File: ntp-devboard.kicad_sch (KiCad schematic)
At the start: 71 parts, among them J1 USB_C_Receptacle_USB2.0_14P, J2 Conn_01x07, J3 Conn_01x20, J4 Conn_01x04, J6 RJ45_Hanrun_HR911105A_Horizon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, SW1 SW_Push, U1 RP2040, U2 MCP1700x-330xxTT, U3 LAN9250/ML, U4 W25Q16JVUXIQ TR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

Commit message: bom optimisation
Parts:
- C37: footprint Capacitor_SMD:C_0402_1005Metric -> Capacitor_SMD:C_0805_2012Metric
- FB1, FB2, FB3, FB4: footprint Inductor_SMD:L_0201_0603Metric -> Inductor_SMD:L_0603_1608Metric
- R11, R12: value 330 -> 10K
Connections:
- no-connect marks 24 -> 23
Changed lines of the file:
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@@
 	)
 	(no_connect
-		(at 25.4 135.89)
-	)
-	(no_connect
 		(at 35.56 254)
 	)
@@
 			)
 		)
-		(property "Value" "330"
+		(property "Value" "10K"
 			(at 151.13 264.16 90)
 			(effects
@@
 			)
 		)
-		(property "Footprint" "Inductor_SMD:L_0201_0603Metric"
+		(property "Footprint" "Inductor_SMD:L_0603_1608Metric"
 			(at 313.182 163.83 90)
 			(effects
@@
 			)
 		)
-		(property "Value" "330"
+		(property "Value" "10K"
 			(at 19.05 228.6 90)
 			(effects
@@
 			)
 		)
-		(property "Footprint" "Inductor_SMD:L_0201_0603Metric"
+		(property "Footprint" "Inductor_SMD:L_0603_1608Metric"
 			(at 245.872 236.22 90)
 			(effects
@@
 			)
 		)
-		(property "Footprint" "Inductor_SMD:L_0201_0603Metric"
+		(property "Footprint" "Inductor_SMD:L_0603_1608Metric"
 			(at 341.122 163.83 90)
 			(effects
@@
 			)
 		)
-		(property "Footprint" "Capacitor_SMD:C_0402_1005Metric"
+		(property "Footprint" "Capacitor_SMD:C_0805_2012Metric"
 			(at 284.1752 240.03 0)
 			(effects
@@
 			)
 		)
-		(property "Footprint" "Inductor_SMD:L_0201_0603Metric"
+		(property "Footprint" "Inductor_SMD:L_0603_1608Metric"
 			(at 328.422 163.83 90)
 			(effects

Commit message: uhm, _minor_ mistake
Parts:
- added J5: Conn_01x02, Connector_PinHeader_2.54mm:PinHeader_1x02_P2.54mm_Vertical, symbol Connector_Generic:Conn_01x02
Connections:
- net GND: no longer J6.10, J6.11
- net LAN45: now also J5.2 (Pin_2); no longer J6.9
- net LAN46: now also J5.1 (Pin_1); no longer J6.12
- no-connect marks 23 -> 28
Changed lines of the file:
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@@
 	)
 	(no_connect
+		(at 224.79 220.98)
+	)
+	(no_connect
 		(at 35.56 251.46)
 	)
@@
 	)
 	(no_connect
+		(at 224.79 218.44)
+	)
+	(no_connect
+		(at 224.79 223.52)
+	)
+	(no_connect
 		(at 35.56 241.3)
 	)
@@
 	)
 	(no_connect
+		(at 224.79 208.28)
+	)
+	(no_connect
 		(at 35.56 215.9)
 	)
@@
 	)
 	(no_connect
+		(at 224.79 210.82)
+	)
+	(no_connect
 		(at 35.56 238.76)
 	)
@@
 		)
 	)
-	(global_label "LAN46"
-		(shape input)
-		(at 224.79 208.28 0)
-		(fields_autoplaced yes)
-		(effects
-			(font
-				(size 1.27 1.27)
-			)
-			(justify left)
-		)
-		(property "Intersheetrefs" "${INTERSHEET_REFS}"
-			(at 233.6414 208.28 0)
-			(effects
-				(font
-					(size 1.27 1.27)
-				)
-				(justify left)
-				(hide yes)
-			)
-		)
-	)
 	(global_label "QSPI_SD0"
 		(shape bidirectional)
@@
 		)
 	)
+	(global_label "LAN45"
+		(shape input)
+		(at 39.37 121.92 180)
+		(fields_autoplaced yes)
+		(effects
+			(font
+				(size 1.27 1.27)
+			)
+			(justify right)
+		)
+		(property "Intersheetrefs" "${INTERSHEET_REFS}"
+			(at 30.5186 121.92 0)
+			(effects
+				(font
+					(size 1.27 1.27)
+				)
+				(justify right)
+				(hide yes)
+			)
+		)
+	)
 	(global_label "GPIO28_ADC2"
 		(shape bidirectional)
@@
 		)
 	)
-	(global_label "LAN45"
-		(shape input)
-		(at 224.79 218.44 0)
-		(fields_autoplaced yes)
-		(effects
-			(font
-				(size 1.27 1.27)
-			)
-			(justify left)
-		)
-		(property "Intersheetrefs" "${INTERSHEET_REFS}"
-			(at 233.6414 218.44 0)
-			(effects
-				(font
-					(size 1.27 1.27)
-				)
-				(justify left)
-				(hide yes)
-			)
-		)
-	)
 	(global_label "GPIO17"
 		(shape bidirectional)
@@
 		)
 	)
+	(global_label "LAN46"
+		(shape input)
+		(at 39.37 119.38 180)
+		(fields_autoplaced yes)
+		(effects
+			(font
+				(size 1.27 1.27)
+			)
+			(justify right)
+		)
+		(property "Intersheetrefs" "${INTERSHEET_REFS}"
+			(at 30.5186 119.38 0)
+			(effects
+				(font
+					(size 1.27 1.27)
+				)
+				(justify right)
+				(hide yes)
+			)
+		)
+	)
 	(global_label "QSPI_SD3"
 		(shape bidirectional)
@@
 	)
 	(symbol
-		(lib_id "power:+3V3")
-		(at 327.66 153.67 0)
+		(lib_id "Connector_Generic:Conn_01x02")
+		(at 44.45 119.38 0)
 		(unit 1)
 		(exclude_from_sim no)
@@
 		(dnp no)
 		(fields_autoplaced yes)
-		(property "Reference" "#PWR046"
-			(at 327.66 157.48 0)
+		(property "Reference" "J5"
+			(at 46.99 119.3799 0)
 			(effects
 				(font
 					(size 1.27 1.27)
 				)
-				(hide yes)
+				(justify left)
 			)
 		)
-		(property "Value" "+3V3"
-			(at 327.66 148.59 0)
+		(property "Value" "Conn_01x02"
+			(at 46.99 121.9199 0)
 			(effects
 				(font
 					(size 1.27 1.27)
 				)
+				(justify left)
 			)
 		)
-		(property "Footprint" ""
-			(at 327.66 153.67 0)
+		(property "Footprint" "Connector_PinHeader_2.54mm:PinHeader_1x02_P2.54mm_Vertical"
+			(at 44.45 119.38 0)
 			(effects
 				(font
@@
 			)
 		)
-		(property "Datasheet" ""
-			(at 327.66 153.67 0)
+		(property "Datasheet" "~"
+			(at 44.45 119.38 0)
 			(effects
 				(font
@@
 			)
 		)
-		(property "Description" "Power symbol creates a global label with name \"+3V3\""
-			(at 327.66 153.67 0)
+		(property "Description" "Generic connector, single row, 01x02, script generated (kicad-library-utils/schlib/autogen/connector/)"
+			(at 44.45 119.38 0)
 			(effects
 				(font
@@
 		(pin "1"
 		)
+		(pin "2"
+		)
 		(instances
-			(project "ntp-devboard"
+			(project ""
 				(path "/8a2a4d17-ab41-4dea-99ab-88cd6502c408"
-					(reference "#PWR046")
+					(reference "J5")
 					(unit 1)
 				)
@@
 	)
 	(symbol
-		(lib_id "Device:R")
-		(at 168.91 194.31 270)
+		(lib_id "power:+3V3")
+		(at 327.66 153.67 0)
 		(unit 1)
 		(exclude_from_sim no)
@@
 		(on_board yes)
 		(dnp no)
-		(property "Reference" "R15"
-			(at 168.91 189.23 90)
+		(fields_autoplaced yes)
+		(property "Reference" "#PWR046"
+			(at 327.66 157.48 0)
 			(effects
 				(font
 					(size 1.27 1.27)
 				)
+				(hide yes)
 			)
 		)
-		(property "Value" "12.1K"
-			(at 168.91 191.77 90)
+		(property "Value" "+3V3"
+			(at 327.66 148.59 0)
 			(effects
 				(font
@@
 			)
 		)
-		(property "Footprint" "Resistor_SMD:R_0402_1005Metric"
-			(at 168.91 192.532 90)
+		(property "Footprint" ""
+			(at 327.66 153.67 0)
 			(effects
 				(font
@@
 			)
 		)
-		(property "Datasheet" "~"
-			(at 168.91 194.31 0)
+		(property "Datasheet" ""
+			(at 327.66 153.67 0)
 			(effects
 				(font
@@
 			)
 		)
-		(property "Description" "Resistor"
-			(at 168.91 194.31 0)
+		(property "Description" "Power symbol creates a global label with name \"+3V3\""
+			(at 327.66 153.67 0)
 			(effects
 				(font
@@
 			)
 		)
-		(pin "2"
-		)
 		(pin "1"
 		)
@@
 			(project "ntp-devboard"
 				(path "/8a2a4d17-ab41-4dea-99ab-88cd6502c408"
-					(reference "R15")
+					(reference "#PWR046")
 					(unit 1)
 				)
@@
 	)
 	(symbol
-		(lib_id "power:GND")
-		(at 224.79 210.82 0)
+		(lib_id "Device:R")
+		(at 168.91 194.31 270)
 		(unit 1)
 		(exclude_from_sim no)
@@
 		(on_board yes)
 		(dnp no)
-		(fields_autoplaced yes)
-		(property "Reference" "#PWR036"
-			(at 224.79 217.17 0)
+		(property "Reference" "R15"
+			(at 168.91 189.23 90)
 			(effects
 				(font
 					(size 1.27 1.27)
 				)
-				(hide yes)
 			)
 		)
-		(property "Value" "GND"
-			(at 224.79 215.9 0)
+		(property "Value" "12.1K"
+			(at 168.91 191.77 90)
 			(effects
 				(font
@@
 			)
 		)
-		(property "Footprint" ""
-			(at 224.79 210.82 0)
+		(property "Footprint" "Resistor_SMD:R_0402_1005Metric"
+			(at 168.91 192.532 90)
 			(effects
 				(font
@@
 			)
 		)
-		(property "Datasheet" ""
-			(at 224.79 210.82 0)
+		(property "Datasheet" "~"
+			(at 168.91 194.31 0)
 			(effects
 				(font
@@
 			)
 		)
-		(property "Description" "Power symbol creates a global label with name \"GND\" , ground"
-			(at 224.79 210.82 0)
+		(property "Description" "Resistor"
+			(at 168.91 194.31 0)
 			(effects
 				(font
@@
 			)
 		)
+		(pin "2"
+		)
 		(pin "1"
 		)
@@
 			(project "ntp-devboard"
 				(path "/8a2a4d17-ab41-4dea-99ab-88cd6502c408"
-					(reference "#PWR036")
+					(reference "R15")
 					(unit 1)
 				)
@@
 					(unit 1)
 				)
-			)
-		)
-	)
-	(symbol
-		(lib_id "power:GND")
-		(at 224.79 220.98 0)
-		(unit 1)
-		(exclude_from_sim no)
-		(in_bom yes)
-		(on_board yes)
-		(dnp no)
-		(fields_autoplaced yes)
-		(property "Reference" "#PWR035"
-			(at 224.79 227.33 0)
-			(effects
-				(font
-					(size 1.27 1.27)
-				)
-				(hide yes)
-			)
-		)
-		(property "Value" "GND"
-			(at 224.79 226.06 0)
-			(effects
-				(font
-					(size 1.27 1.27)
-				)
-			)
-		)
-		(property "Footprint" ""
-			(at 224.79 220.98 0)
-			(effects
-				(font
-					(size 1.27 1.27)
-				)
-				(hide yes)
-			)
-		)
-		(property "Datasheet" ""
-			(at 224.79 220.98 0)
-			(effects
-				(font
-					(size 1.27 1.27)
-				)
-				(hide yes)
-			)
-		)
-		(property "Description" "Power symbol creates a global label with name \"GND\" , ground"
-			(at 224.79 220.98 0)
-			(effects
-				(font
-					(size 1.27 1.27)
-				)
-				(hide yes)
-			)
-		)
-		(pin "1"
-		)
-		(instances
-			(project "ntp-devboard"
-				(path "/8a2a4d17-ab41-4dea-99ab-88cd6502c408"
-					(reference "#PWR035")
-					(unit 1)
-				)

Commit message: cooked ah decoupling caps
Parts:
- C18, C19: value 33pF -> 15pF
- R15: value 12.1K -> 12K
- R3, R4: value 27 -> 22
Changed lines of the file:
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@@
 			)
 		)
-		(property "Value" "27"
+		(property "Value" "22"
 			(at 133.35 68.834 90)
 			(effects
@@
 			)
 		)
-		(property "Value" "27"
+		(property "Value" "22"
 			(at 133.35 77.216 90)
 			(effects
@@
 			)
 		)
-		(property "Value" "12.1K"
+		(property "Value" "12K"
 			(at 168.91 191.77 90)
 			(effects
@@
 			)
 		)
-		(property "Value" "33pF"
+		(property "Value" "15pF"
 			(at 233.68 138.684 90)
 			(effects
@@
 			)
 		)
-		(property "Value" "33pF"
+		(property "Value" "15pF"
 			(at 233.68 148.844 90)
 			(effects

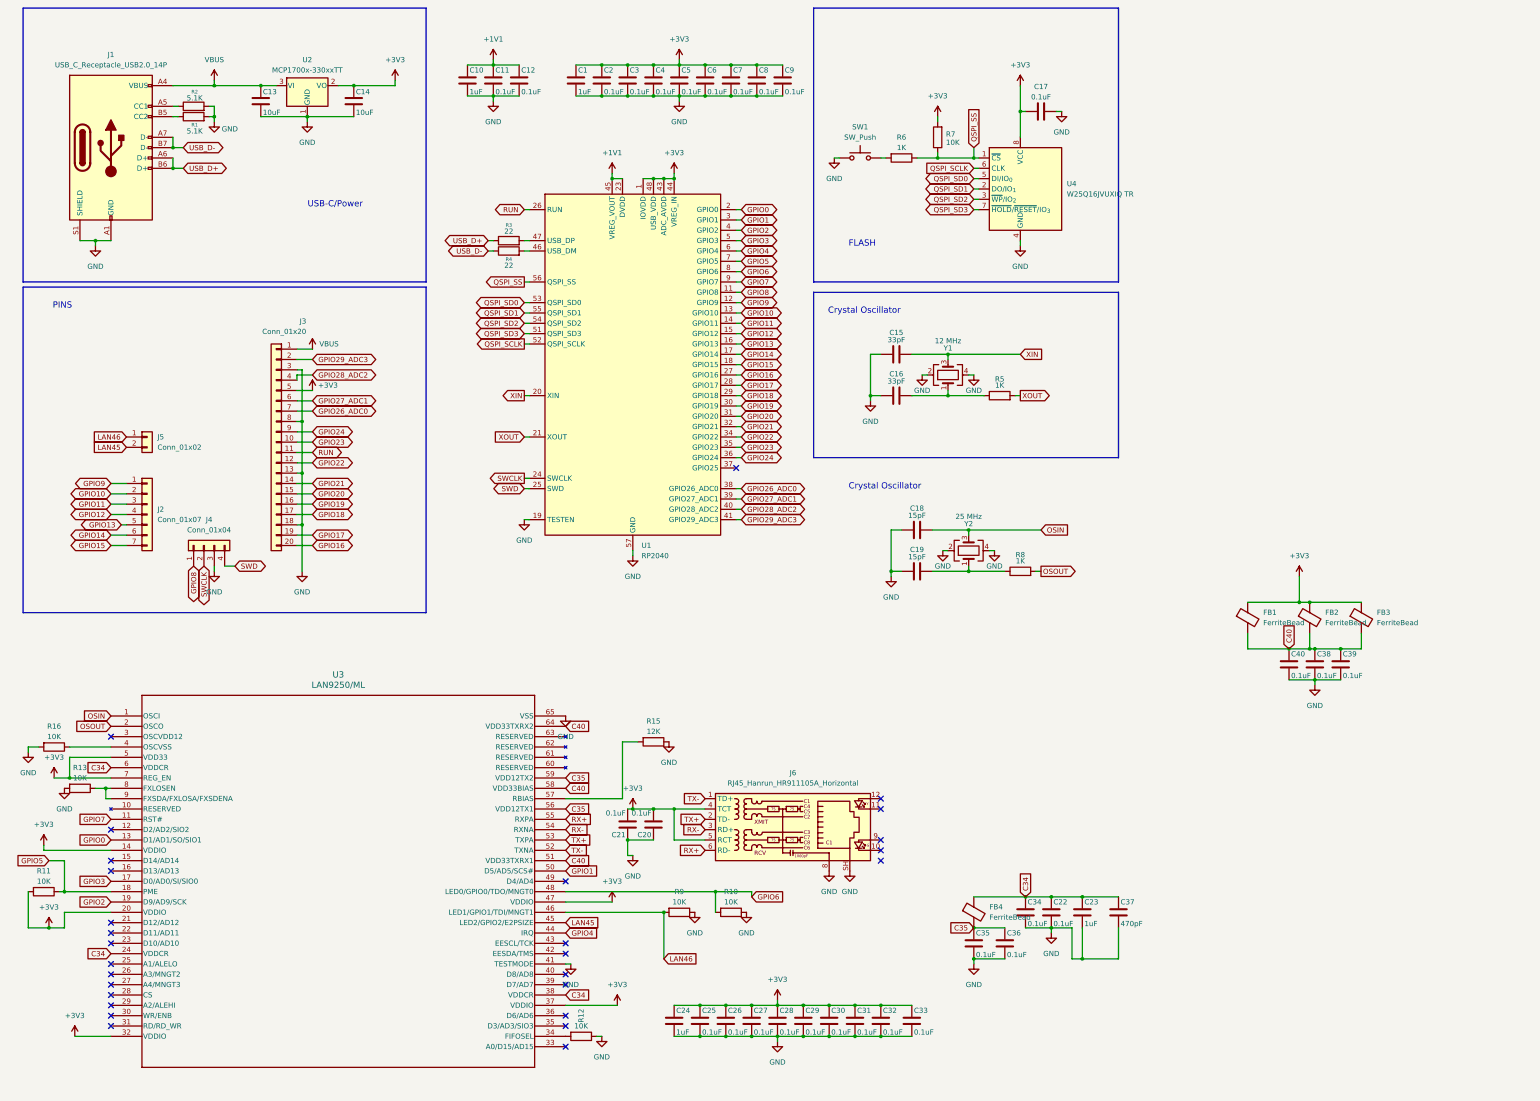
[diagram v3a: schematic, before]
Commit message: Improved schematic readbility
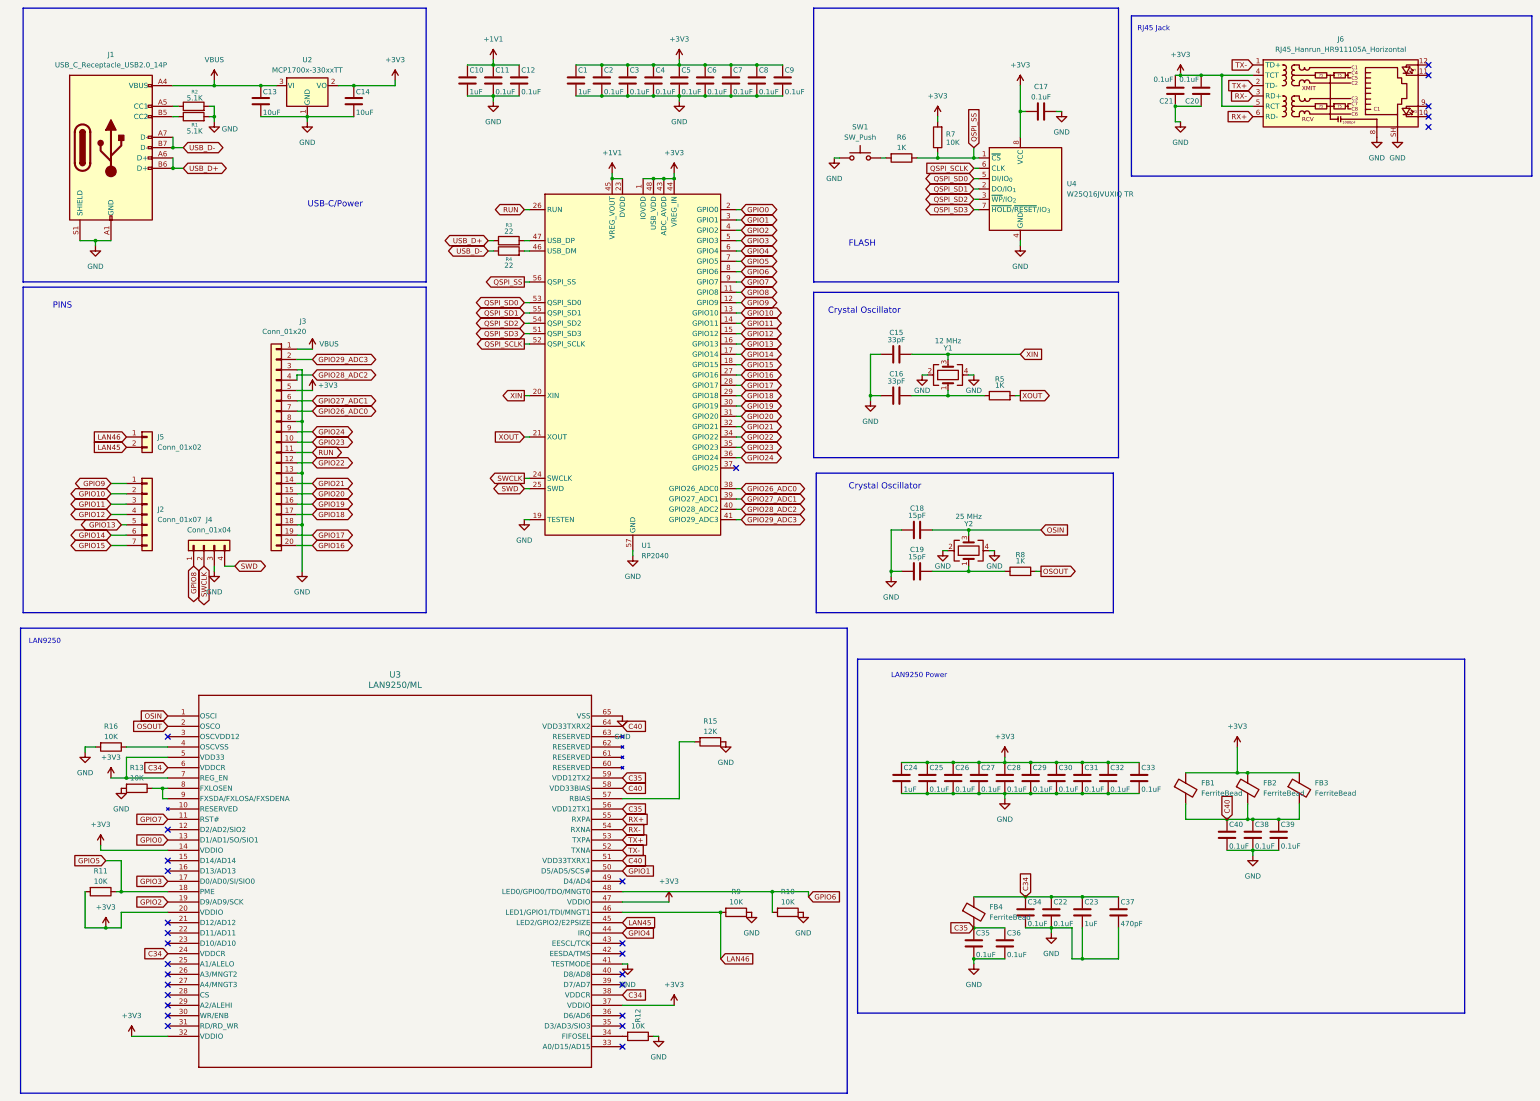
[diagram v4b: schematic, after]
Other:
- note added: "LAN9250"
- note added: "LAN9250 Power"
- note added: "RJ45 Jack"
- moved on the sheet: C20, C21, C24, C25, C26, C27, C28, C29, C30, C31, C32, C33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

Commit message: update sch and pcb
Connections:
- net GND: now also R13.1; no longer R13.2
- net at U3.8 (FXLOSEN), U3.9 (FXSDA/FXLOSA/FXSDENA): now also R13.2; no longer R13.1
- net C34 renamed Power_Lan
- net C35 renamed POWER_LAN12
- net C40 renamed TXRX_POWER
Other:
- moved on the sheet: R13
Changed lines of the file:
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@@
 		)
 	)
-	(global_label "C34"
+	(global_label "Power_Lan"
 		(shape input)
 		(at 161.29 256.54 0)
@@
 		)
 		(property "Intersheetrefs" "${INTERSHEET_REFS}"
-			(at 167.9642 256.54 0)
+			(at 174.1932 256.54 0)
 			(effects
 				(font
@@
 		)
 	)
-	(global_label "C40"
+	(global_label "TXRX_POWER"
 		(shape input)
 		(at 161.29 223.52 0)
@@
 		)
 		(property "Intersheetrefs" "${INTERSHEET_REFS}"
-			(at 167.9642 223.52 0)
+			(at 176.3703 223.52 0)
 			(effects
 				(font
@@
 		)
 	)
-	(global_label "C40"
+	(global_label "TXRX_POWER"
 		(shape input)
 		(at 309.88 213.36 90)
@@
 		)
 		(property "Intersheetrefs" "${INTERSHEET_REFS}"
-			(at 309.88 206.6858 90)
+			(at 309.88 198.2797 90)
 			(effects
 				(font
@@
 		)
 	)
-	(global_label "C40"
+	(global_label "TXRX_POWER"
 		(shape input)
 		(at 161.29 190.5 0)
@@
 		)
 		(property "Intersheetrefs" "${INTERSHEET_REFS}"
-			(at 167.9642 190.5 0)
+			(at 176.3703 190.5 0)
 			(effects
 				(font
@@
 		)
 	)
-	(global_label "C34"
+	(global_label "Power_Lan"
 		(shape input)
 		(at 260.35 232.41 90)
@@
 		)
 		(property "Intersheetrefs" "${INTERSHEET_REFS}"
-			(at 260.35 225.7358 90)
+			(at 260.35 219.5068 90)
 			(effects
 				(font
@@
 		)
 	)
-	(global_label "C35"
+	(global_label "POWER_LAN12"
 		(shape input)
 		(at 161.29 203.2 0)
@@
 		)
 		(property "Intersheetrefs" "${INTERSHEET_REFS}"
-			(at 167.9642 203.2 0)
+			(at 177.5799 203.2 0)
 			(effects
 				(font
@@
 		)
 	)
-	(global_label "C34"
+	(global_label "Power_Lan"
 		(shape input)
 		(at 49.53 246.38 180)
@@
 		)
 		(property "Intersheetrefs" "${INTERSHEET_REFS}"
-			(at 42.8558 246.38 0)
+			(at 36.6268 246.38 0)
 			(effects
 				(font
@@
 		)
 	)
-	(global_label "C35"
+	(global_label "POWER_LAN12"
 		(shape input)
 		(at 161.29 210.82 0)
@@
 		)
 		(property "Intersheetrefs" "${INTERSHEET_REFS}"
-			(at 167.9642 210.82 0)
+			(at 177.5799 210.82 0)
 			(effects
 				(font
@@
 		)
 	)
-	(global_label "C35"
+	(global_label "POWER_LAN12"
 		(shape input)
 		(at 247.65 240.03 180)
@@
 		)
 		(property "Intersheetrefs" "${INTERSHEET_REFS}"
-			(at 240.9758 240.03 0)
+			(at 231.3601 240.03 0)
 			(effects
 				(font
@@
 		)
 	)
-	(global_label "C40"
+	(global_label "TXRX_POWER"
 		(shape input)
 		(at 161.29 205.74 0)
@@
 		)
 		(property "Intersheetrefs" "${INTERSHEET_REFS}"
-			(at 167.9642 205.74 0)
+			(at 176.3703 205.74 0)
 			(effects
 				(font
@@
 		)
 	)
-	(global_label "C34"
+	(global_label "Power_Lan"
 		(shape input)
 		(at 49.53 200.66 180)
@@
 		)
 		(property "Intersheetrefs" "${INTERSHEET_REFS}"
-			(at 42.8558 200.66 0)
+			(at 36.6268 200.66 0)
 			(effects
 				(font
@@
 	(symbol
 		(lib_id "Device:R")
-		(at 41.91 205.74 270)
+		(at 41.91 205.74 90)
 		(unit 1)
 		(exclude_from_sim no)
@@
 		(dnp no)
 		(property "Reference" "R13"
-			(at 41.91 200.66 90)
+			(at 41.91 210.82 90)
 			(effects
 				(font
@@
 		)
 		(property "Value" "10K"
-			(at 41.91 203.2 90)
+			(at 41.91 208.28 90)
 			(effects
 				(font
@@
 		)
 		(property "Footprint" "Resistor_SMD:R_0402_1005Metric"
-			(at 41.91 203.962 90)
+			(at 41.91 207.518 90)
 			(effects
 				(font
